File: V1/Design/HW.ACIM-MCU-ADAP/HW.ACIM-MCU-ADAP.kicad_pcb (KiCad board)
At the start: 4 copper layers, 81 x 67.8 mm, 116 parts, among them J1 U, J101 HEADER 2x15POS, J102 HEADER 2x15POS, J2 V, J3 W, J4 PGND, U1 ISO OPAMP 1-CH, U101 MIPS 32-bit DSC, U102 12MHz, U15 ISO OPAMP 1-CH, U17 OP-1CH, U2 ISO OPAMP 1-CH, U3 OP-1CH, U4 OP-1CH, U5 LDO 3.3V

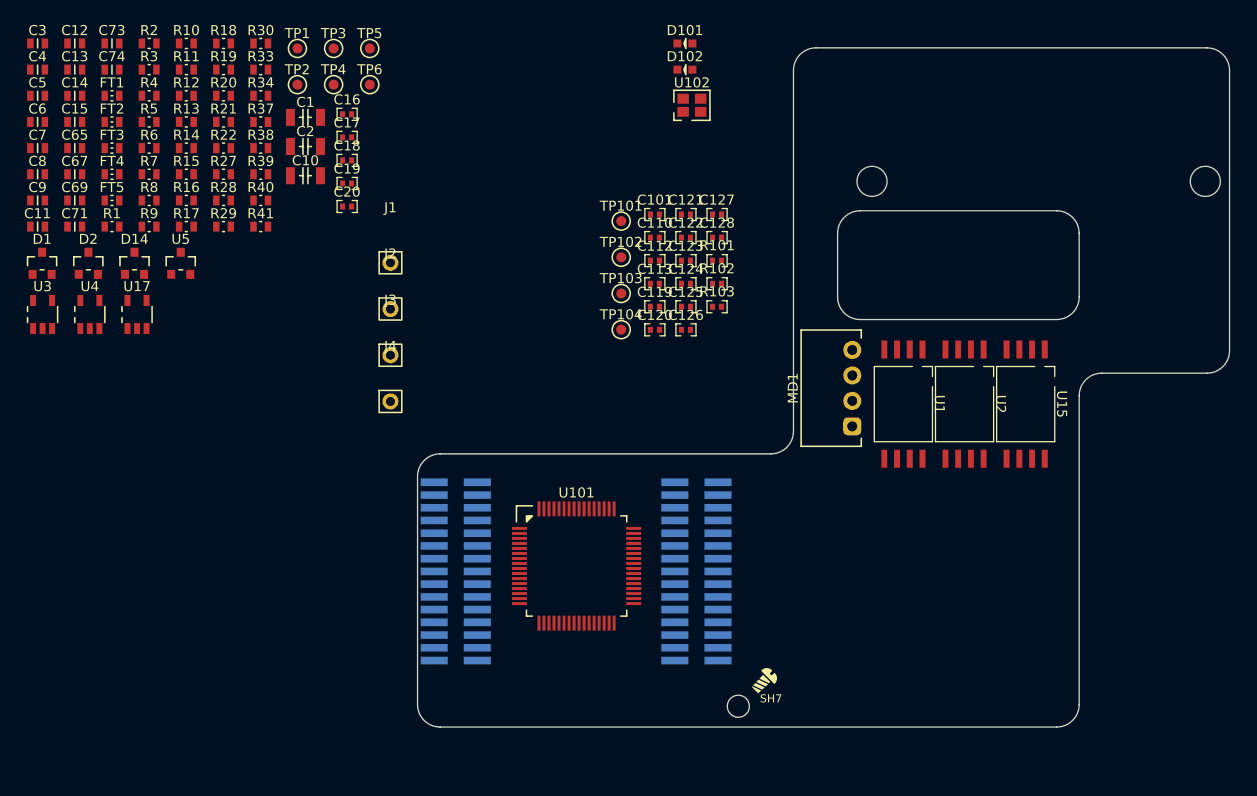
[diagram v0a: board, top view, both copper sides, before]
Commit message: HW.ACIM-MCU-ADAP schematic update 1
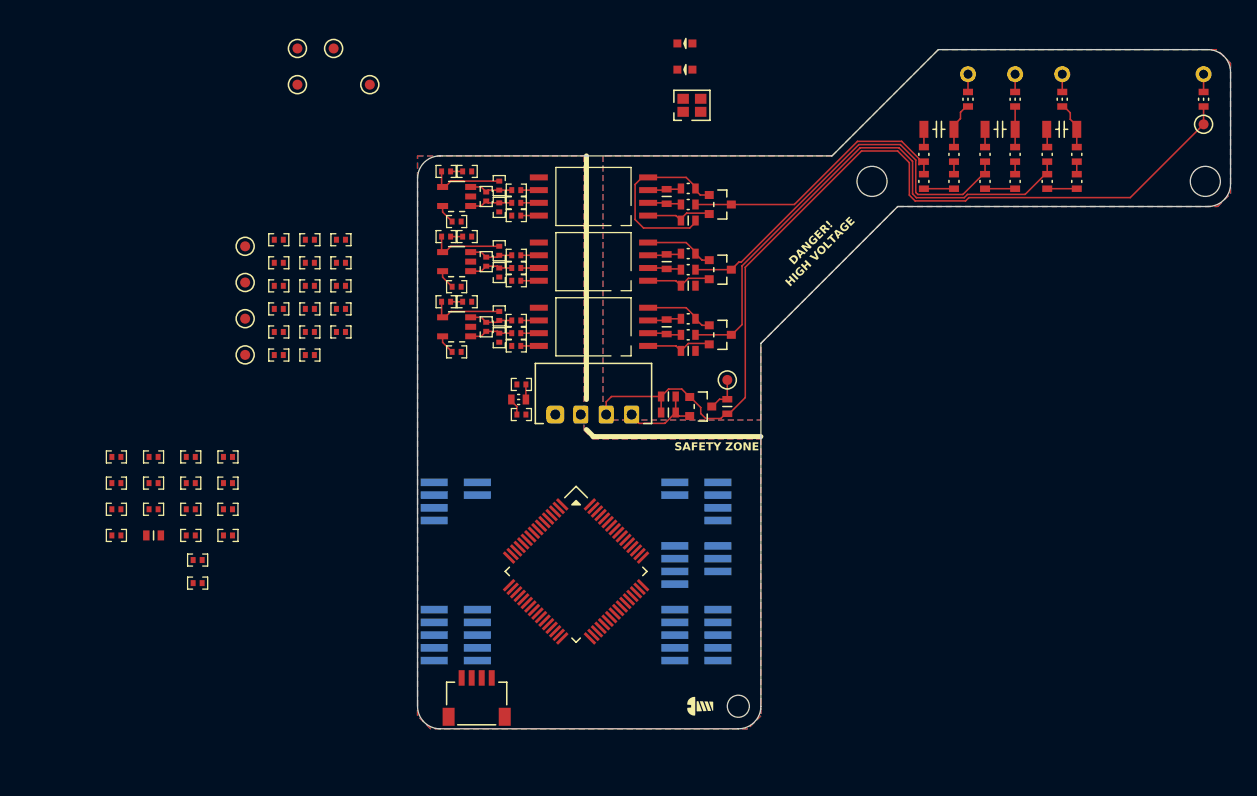
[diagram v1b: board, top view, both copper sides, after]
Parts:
- added C21: 1nF, SAMPI:CAP0402, F.Cu at (167.1, 86.1)
- added C22: 1nF, SAMPI:CAP0402, F.Cu at (167.1, 88.7)
- added C23: 1nF, SAMPI:CAP0402, F.Cu at (167.1, 91.4)
- added C24: 1nF, SAMPI:CAP0402, F.Cu at (167.1, 94.0)
- added C25: 1nF, SAMPI:CAP0402, F.Cu at (170.9, 86.1)
- added C26: 1nF, SAMPI:CAP0402, F.Cu at (170.9, 88.7)
- added C27: 1nF, SAMPI:CAP0402, F.Cu at (170.9, 91.4)
- added C28: 1nF, SAMPI:CAP0603, F.Cu at (170.9, 94.0)
- added FT10: 1K@100MHz, SAMPI:IND0402, F.Cu at (178.3, 86.1)
- added FT11: 1K@100MHz, SAMPI:IND0402, F.Cu at (178.3, 88.7)
- added FT12: 1K@100MHz, SAMPI:IND0402, F.Cu at (178.3, 91.4)
- added FT13: 1K@100MHz, SAMPI:IND0402, F.Cu at (178.3, 94.0)
- added FT6: 1K@100MHz, SAMPI:IND0402, F.Cu at (174.6, 86.1)
- added FT7: 1K@100MHz, SAMPI:IND0402, F.Cu at (174.6, 88.7)
- added FT8: 1K@100MHz, SAMPI:IND0402, F.Cu at (174.6, 91.4)
- added FT9: 1K@100MHz, SAMPI:IND0402, F.Cu at (174.6, 94.0)
- added J5: QWIIC, SAMPI:HDM-1x4x1.0-RA, F.Cu at (203.1, 111.0)
- added R23: 10K, SAMPI:RES0402, F.Cu at (175.3, 96.4)
- added R24: 10K, SAMPI:RES0402, F.Cu at (175.3, 98.7)
- C11, C12, C13, C14, C15, C69, C7, C71, C73, C74, C8, C9: footprint SAMPI:CAP0603 -> SAMPI:CAP0402
- C16, C17, C18: footprint SAMPI:CAP0402 -> SAMPI:CAP0603
- J1, J2, J3, J4: moved to B.Cu
- R13, R14, R15, R16, R17, R18, R19, R20, R21, R22, R37, R38, R39, R40, R41: footprint SAMPI:RES0603 -> SAMPI:RES0402
- U102: value 12MHz -> 24MHz
- moved FT4 109.1 mm to (275.6, 50.5), turned to -90 degrees
- moved FT3 94.9 mm to (261.5, 50.5), turned to -90 degrees
- moved R6 92.6 mm to (262.9, 58.7), turned to -90 degrees
- moved R5 92.6 mm to (262.9, 56.0), turned to -90 degrees
- moved R1 90.4 mm to (256.8, 56.0), turned to -90 degrees
- moved FT2 90.1 mm to (256.8, 50.5), turned to -90 degrees
- moved R8 89.7 mm to (260.0, 56.0), turned to 90 degrees
- moved R7 89.6 mm to (260.0, 58.7), turned to 90 degrees
- moved R2 87.5 mm to (256.8, 58.7), turned to -90 degrees
- moved J4 87.4 mm to (275.6, 48.0), turned to 180 degrees
- moved TP4 86.9 mm to (275.6, 53.0)
- moved FT1 85.4 mm to (252.1, 50.5), turned to -90 degrees
- moved R3 84.1 mm to (253.8, 58.7), turned to 90 degrees
- moved R4 83.6 mm to (253.8, 56.0), turned to 90 degrees
- moved C2 75.5 mm to (261.4, 53.5), turned to 180 degrees
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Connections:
- net /MCU/IO1 renamed /MCU/IND_RUN
- net /MCU/IO2 renamed /MCU/IND_ERR
- net /VOLTAGE MEASUREMENT/MC_UU_DIV renamed /MCU/MC_UU
- net /VOLTAGE MEASUREMENT/MC_UV_DIV renamed /MCU/MC_UV
- net /VOLTAGE MEASUREMENT/MC_UW_DIV renamed /MCU/MC_UW
- C1 pad 2: PGND -> GND_ISO
- C10 pad 2: PGND -> GND_ISO
- C112 pad 2: AVDD_MCU -> Net-(U101-AVDD)
- C113 pad 2: AVDD_MCU -> Net-(U101-AVDD)
- C2 pad 2: PGND -> GND_ISO
- J101 pad 23: /MCU/VDC_DIV -> /MCU/UDC
- J101 pad 25: /MCU/IDC_SEN -> /MCU/IDC
- J102 pad 16: /MCU/MC_PWM_WL -> /MCU/MC_PWM_VL
- J102 pad 18: /MCU/MC_PWM_VL -> /MCU/MC_PWM_WL
- J102 pad 24: /MCU/MC_IU_SEN -> /MCU/MC_IU
- J102 pad 26: /MCU/MC_IV_SEN -> /MCU/MC_IW
- U101 pad 1: /MCU/~{PFC_FLT} -> unconnected-(U101-TCK/RPA7/PWM10H/PWM4L/PMD5/RA7-Pad1)
- U101 pad 11: /MCU/PFC_PWM_ENA -> unconnected-(U101-AN10/CVD10/RPA12/RA12-Pad11)
- U101 pad 12: /MCU/PFC_PWM_ENB -> unconnected-(U101-AN9/CVD9/RPA11/RA11-Pad12)
- U101 pad 13: /MCU/PFC_IA_SEN -> /MCU/MC_UU_DIV
- U101 pad 14: /MCU/PFC_IB_SEN -> /MCU/MC_UV_DIV
- U101 pad 16: /MCU/MC_VU_DIV -> unconnected-(U101-PGC3/OA1OUT/VREF+/AN3/C1IN4-/C4IN2-/RPB1/CTED1/RB1-Pad16)
- U101 pad 18: /MCU/VAC_DIV -> /MCU/MC_UW_DIV
- U101 pad 19: AVDD_MCU -> Net-(U101-AVDD)
- U101 pad 2: /MCU/PFC_PWM_A -> unconnected-(U101-RPB14/PWM1H/VBUSON1/PMD6/RB14-Pad2)
- U101 pad 21: /MCU/VDC_DIV -> /MCU/UDC_DIV
- U101 pad 23: /MCU/MC_VV_DIV -> unconnected-(U101-OA3IN+/AN8/CVD8/C3IN1+/C3IN3-/RPC2/FLT3/PMA13/RC2-Pad23)
- U101 pad 29: /MCU/DV_CTS -> unconnected-(U101-AN14/CVD14/RPE14/FLT7/PMA1/RE14-Pad29)
- U101 pad 3: /MCU/PFC_PWM_B -> unconnected-(U101-RPB15/PWM7H/PWM1L/PMD7/RB15-Pad3)
- U101 pad 30: /MCU/MC_VR_DIV -> unconnected-(U101-AN15/CVD15/RPE15/FLT8/PMA0/RE15-Pad30)
- U101 pad 31: /MCU/MC_IV_SEN -> /MCU/MC_IW_SEN
- U101 pad 32: /MCU/DV_RTS -> unconnected-(U101-FLT15/RPB4/SCL2/PMA8/RB4-Pad32)
- U101 pad 49: /MCU/MC_TEMP_SEN -> unconnected-(U101-TMS/OA5IN-/AN27/CVD27/LVDIN/C5IN1-/RPB9/RB9-Pad49)
- U101 pad 58: /MCU/~{BUTTON} -> unconnected-(U101-RPF0/PWM11H/RF0-Pad58)
- U101 pad 60: /MCU/SDI -> unconnected-(U101-RPB10/PWM3H/PMD0/RB10-Pad60)
- U101 pad 61: /MCU/SCK -> unconnected-(U101-RPB11/PWM9H/PWM3L/PMD1/RB11-Pad61)
- U101 pad 63: /MCU/SDO -> unconnected-(U101-RPB13/PWM8H/PWM2L/CTPLS/PMD3/RB13-Pad63)
- U101 pad 64: /MCU/~{CS} -> unconnected-(U101-TDO/PWM4H/PMD4/RA10-Pad64)
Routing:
- net GND_ISO: track 0.00 -> 130.2 mm
- net Net-(D2-COM): track 0.00 -> 52.4 mm
- net Net-(D1-COM): track 0.00 -> 40.1 mm
- net Net-(D14-COM): track 0.00 -> 28.1 mm
- net +3V3_ISO: track 0.00 -> 23.8 mm
- net +3V3_MCU: track 0.00 -> 13.0 mm
- net Net-(MD1-DC+): track 0.00 -> 8.44 mm
- net Net-(U17-OUT): track 0.00 -> 7.48 mm
- net Net-(U4-OUT): track 0.00 -> 7.48 mm
- net Net-(U3-OUT): track 0.00 -> 7.48 mm
- net Net-(C2-Pad1): track 0.00 -> 4.75 mm
- net Net-(C10-Pad1): track 0.00 -> 4.73 mm
- net Net-(U17-IN+): track 0.00 -> 4.38 mm
- net Net-(U4-IN-): track 0.00 -> 4.38 mm
- net Net-(U4-IN+): track 0.00 -> 4.38 mm
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- added copper zone on B.Cu, net GND_ISO
- added copper zone on F.Cu, net GND_ISO
- added copper zone on In1.Cu, net GND_ISO
- added copper zone on In2.Cu, net GND_ISO
- added copper zone on B.Cu, net GND_MCU
- added copper zone on F.Cu, net GND_MCU
- added copper zone on In1.Cu, net GND_MCU
- added copper zone on In2.Cu, net GND_MCU
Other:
- board size 81 x 67.8 mm -> 81.1 x 67.8 mm
- board text added: "DANGER! HIGH VOLTAGE"
- board text added: "SAFETY ZONE"

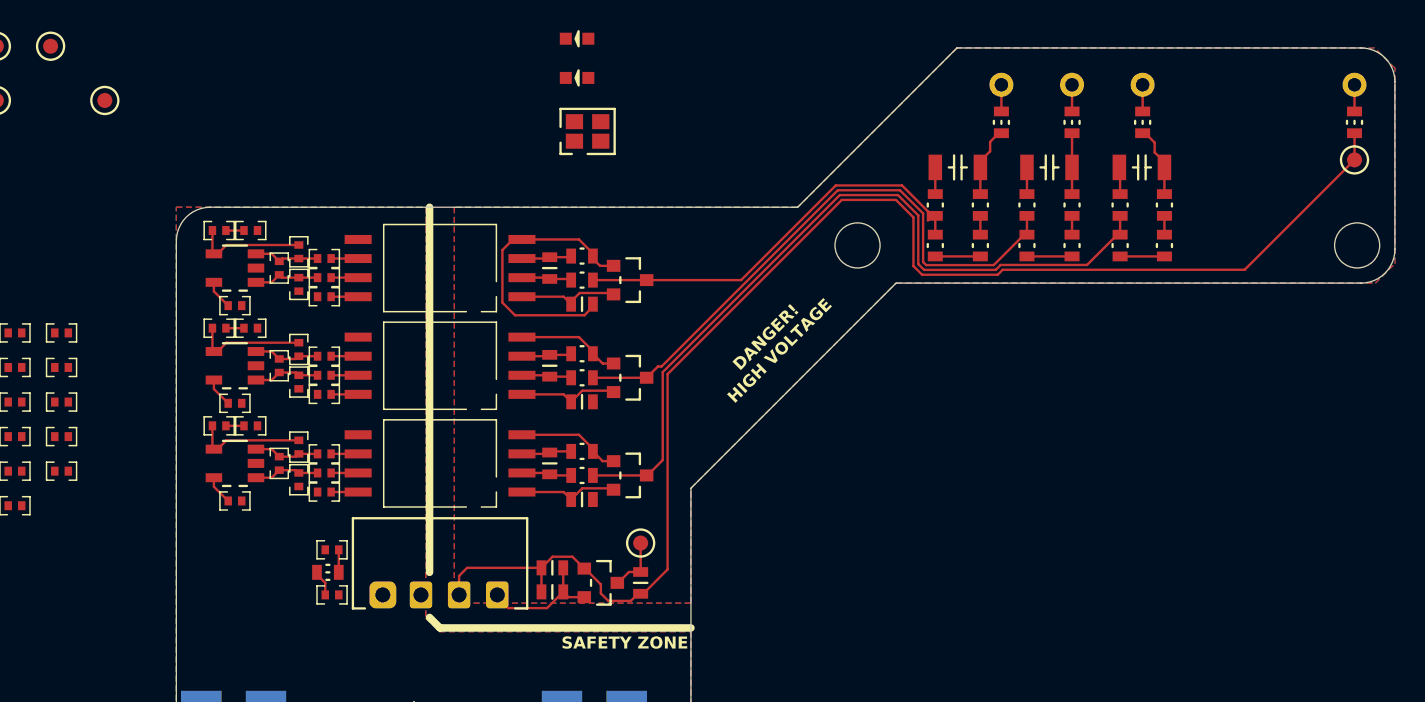
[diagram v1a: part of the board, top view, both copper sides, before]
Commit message: HW.ACIM-MCU-ADAP schematic update 2
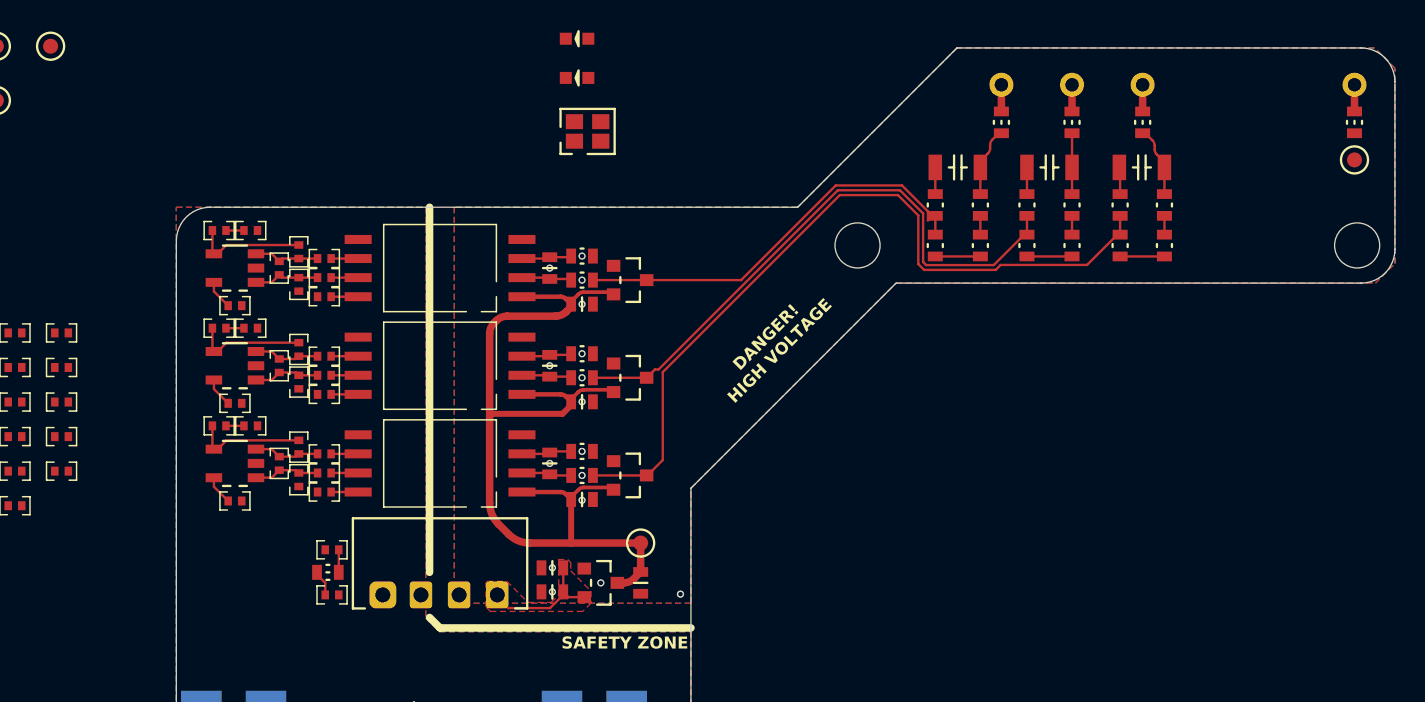
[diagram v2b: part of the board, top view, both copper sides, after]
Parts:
- removed TP6: 5V ISO, SAMPI:TP1MM
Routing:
- net GND_ISO: track 130.2 -> 5.35 mm, vias 0 -> 16
- net +3V3_ISO: track 23.8 -> 62.0 mm
- added copper zone on F.Cu, net Net-(MD1-DC+)

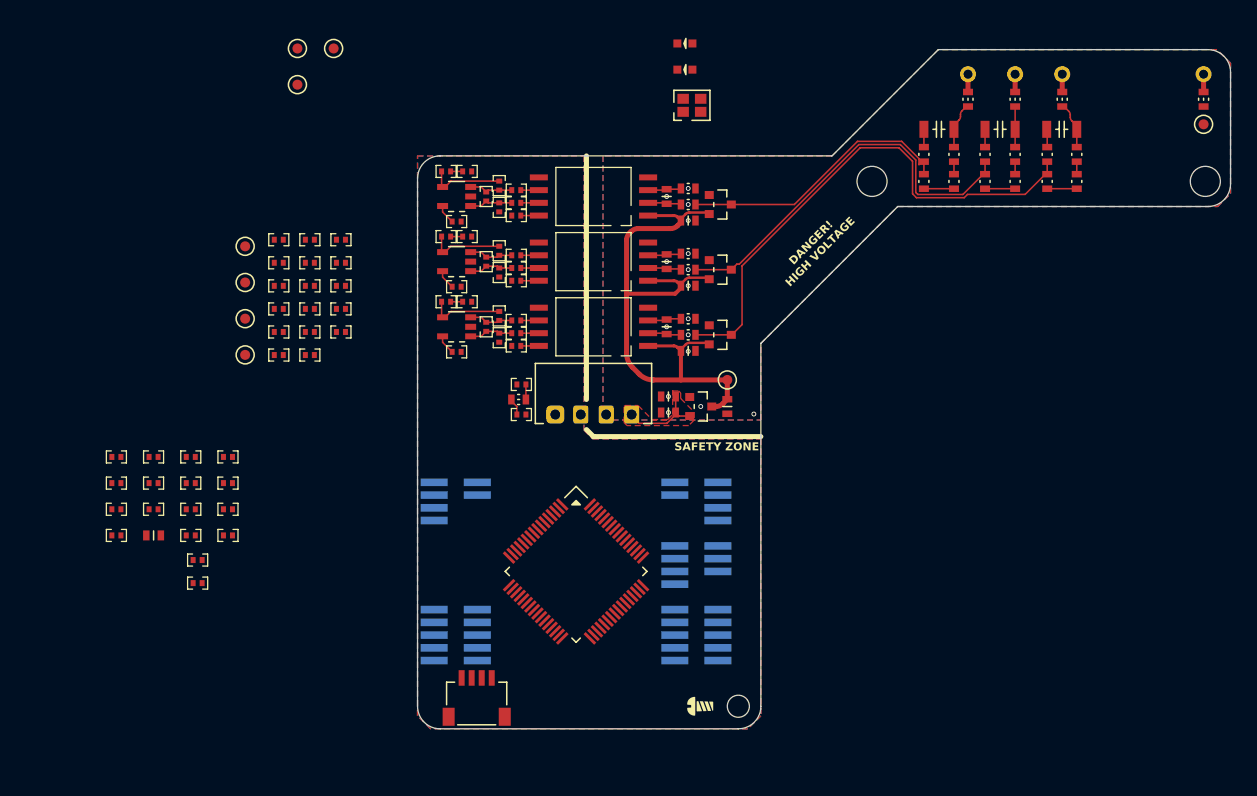
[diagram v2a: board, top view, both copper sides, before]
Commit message: HW.ACIM-MCU-ADAP schematic update 3
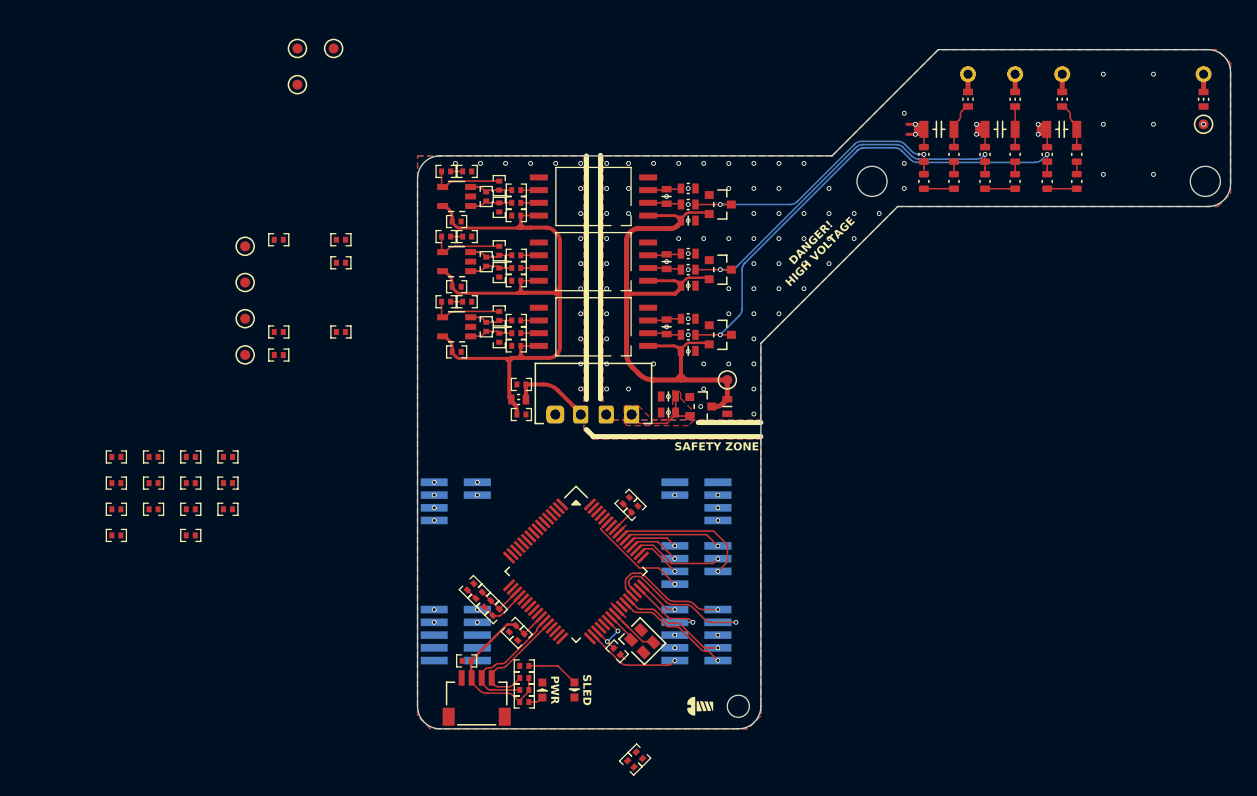
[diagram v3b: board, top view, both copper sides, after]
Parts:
- added C29: 10uF, SAMPI:CAP0402, F.Cu at (202.1, 106.5)
- C28: footprint SAMPI:CAP0603 -> SAMPI:CAP0402
- R23, R24: value 10K -> 2.2K
- moved D101 65.4 mm to (212.8, 109.4), turned to 90 degrees
- moved D102 63.5 mm to (209.6, 109.4), turned to -90 degrees
- moved C123 57.4 mm to (218.5, 116.7), turned to 135 degrees
- moved C124 55.3 mm to (219.3, 115.9), turned to 135 degrees
- moved U102 53.7 mm to (219.6, 104.5), turned to -45 degrees
- moved C110 51.4 mm to (217.1, 105.5), turned to 135 degrees
- moved R102 43.3 mm to (207.8, 110.6), turned to 180 degrees
- moved C121 42.1 mm to (218.9, 91.3), turned to -135 degrees
- moved R101 42.1 mm to (207.8, 107.0), turned to 180 degrees
- moved C122 39.5 mm to (218.0, 90.5), turned to -135 degrees
- moved C112 39.1 mm to (205.0, 101.6), turned to 45 degrees
- moved C113 36.0 mm to (204.2, 100.8), turned to 45 degrees
- moved C125 35.8 mm to (206.7, 103.3), turned to 45 degrees
- moved C126 35.1 mm to (207.5, 104.1), turned to 45 degrees
- moved R23 34.6 mm to (207.8, 108.2)
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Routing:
- net +3V3_MCU: track 13.0 -> 104.9 mm, vias 0 -> 4
- net GND_ISO: track 5.35 -> 21.8 mm, vias 16 -> 89
- net /MCU/DB_TXD: track 0.00 -> 15.8 mm, vias 0 -> 1
- net /MCU/MC_PWM_VL: track 0.00 -> 14.4 mm, vias 0 -> 1
- net /MCU/SDA: track 0.00 -> 13.5 mm
- net /MCU/DV_TXD: track 0.00 -> 12.7 mm, vias 0 -> 1
- net /MCU/SCL: track 0.00 -> 11.7 mm
- net /MCU/PGD: track 0.00 -> 11.5 mm, vias 0 -> 1
- net /MCU/PGC: track 0.00 -> 10.8 mm, vias 0 -> 1
- net /MCU/~{INV_FLT}: track 0.00 -> 10.7 mm, vias 0 -> 1
- net /MCU/MC_PWM_UL: track 0.00 -> 9.92 mm, vias 0 -> 1
- net /MCU/VBUS: track 0.00 -> 9.52 mm, vias 0 -> 1
- net /MCU/MC_PWM_WL: track 0.00 -> 9.35 mm, vias 0 -> 1
- net /MCU/DB_RXD: track 0.00 -> 8.46 mm, vias 0 -> 1
- net Net-(MD1-VI+): track 1.50 -> 8.19 mm
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
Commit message: HW.ACIM-MCU-ADAP schematic update 4
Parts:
- added TP6: UU DIV, SAMPI:TP1MM, F.Cu at (230.4, 61.0)
- added TP7: UV DIV, SAMPI:TP1MM, F.Cu at (230.4, 67.5)
- added TP8: UW DIV, SAMPI:TP1MM, F.Cu at (230.4, 74.0)
- moved C120 48.8 mm to (221.5, 106.4), turned to 45 degrees
- moved C119 47.5 mm to (218.0, 106.2), turned to 135 degrees
- moved C24 43.1 mm to (208.7, 105.3), turned to 45 degrees
- moved FT9 37.0 mm to (209.6, 106.2), turned to 45 degrees
- moved C127 32.3 mm to (206.4, 92.1), turned to -45 degrees
- moved C128 30.7 mm to (205.6, 92.9), turned to -45 degrees
- moved C123 10.5 mm to (215.1, 106.9), turned to 90 degrees
- moved C124 9.54 mm to (216.3, 106.9), turned to 90 degrees
- moved R101 4.82 mm to (212.7, 106.9), turned to 90 degrees
- moved C110 3.50 mm to (213.9, 106.9), turned to 90 degrees
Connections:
- C14 pad 1: GND_ADC -> AGND_MCU
- C15 pad 1: GND_ADC -> AGND_MCU
- C74 pad 1: GND_ADC -> AGND_MCU
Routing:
- net AGND_MCU: track 4.73 -> 37.4 mm, vias 0 -> 5
- net /MCU/MC_IW: track 0.00 -> 29.4 mm, vias 1 -> 2
- net +3V3_MCU: track 104.9 -> 118.9 mm, vias 4 -> 2
- net AVDD_MCU: track 1.20 -> 14.2 mm, vias 0 -> 1
- net /MCU/ENC_IDX: track 0.00 -> 12.5 mm
- net /MCU/ENC_HOME: track 0.00 -> 11.6 mm
- net /MCU/ENC_A: track 0.00 -> 11.5 mm
- net /MCU/IND_RUN: track 0.00 -> 10.7 mm
- net /MCU/USB_N: track 0.00 -> 10.6 mm
- net /MCU/USB_P: track 0.00 -> 10.3 mm
- net /MCU/SLED: track 0.00 -> 9.95 mm
- net /MCU/ENC_B: track 0.00 -> 9.01 mm
- net /MCU/IND_ERR: track 0.00 -> 5.59 mm
- net /MCU/DEV_RELAY: track 0.00 -> 4.13 mm, vias 1 -> 2
- net GND_MCU: track 3.81 -> 7.92 mm, vias 15 -> 19
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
